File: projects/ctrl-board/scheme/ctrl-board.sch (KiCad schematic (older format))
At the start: 121 parts, among them K1 i2c-1, K2 i2c-1, P1 PWR-IN, P2 CONN_4, P3 PWR-IN, P4 PWR-IN, P5 PWR-IN, P6 CONN_4, P7 CONN_4, P8 PWR-IN, Q1 BC847, Q10 BC847, Q11 MOS_P, Q12 MOS_P, Q13 MOS_P, Q2 BC847, Q3 BC847, Q4 BC857, Q5 MOS_P, Q6 MOS_N, Q7 BC847, Q8 BC847, Q9 BC857, U1 NCP3063, U2 L293, X1 8MHz

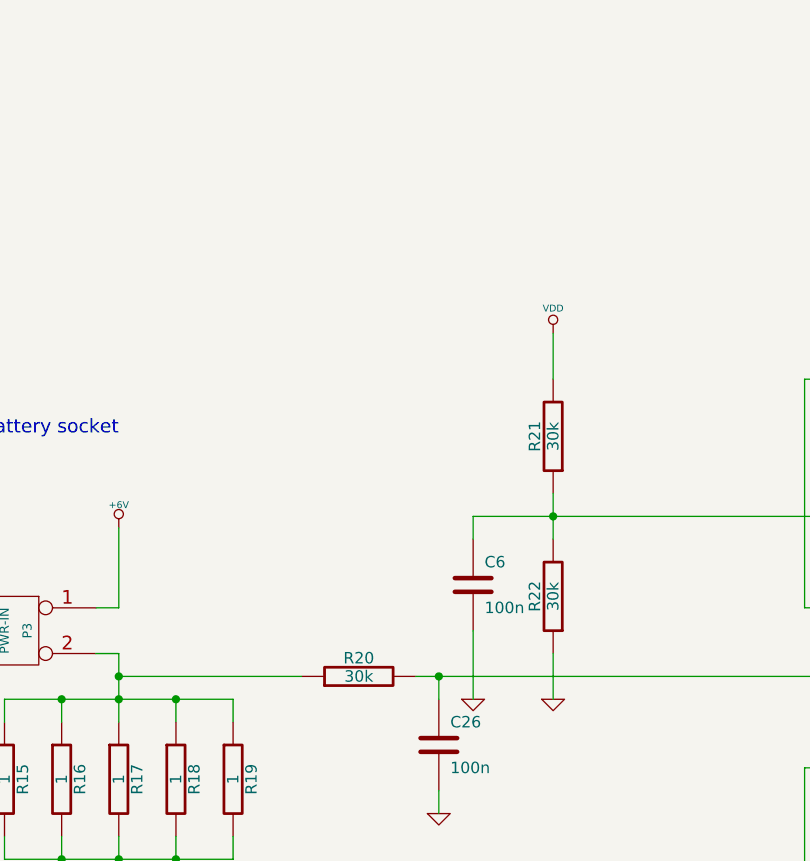
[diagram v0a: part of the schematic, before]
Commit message: Rerouted with eliminating error with measuring consuming current.
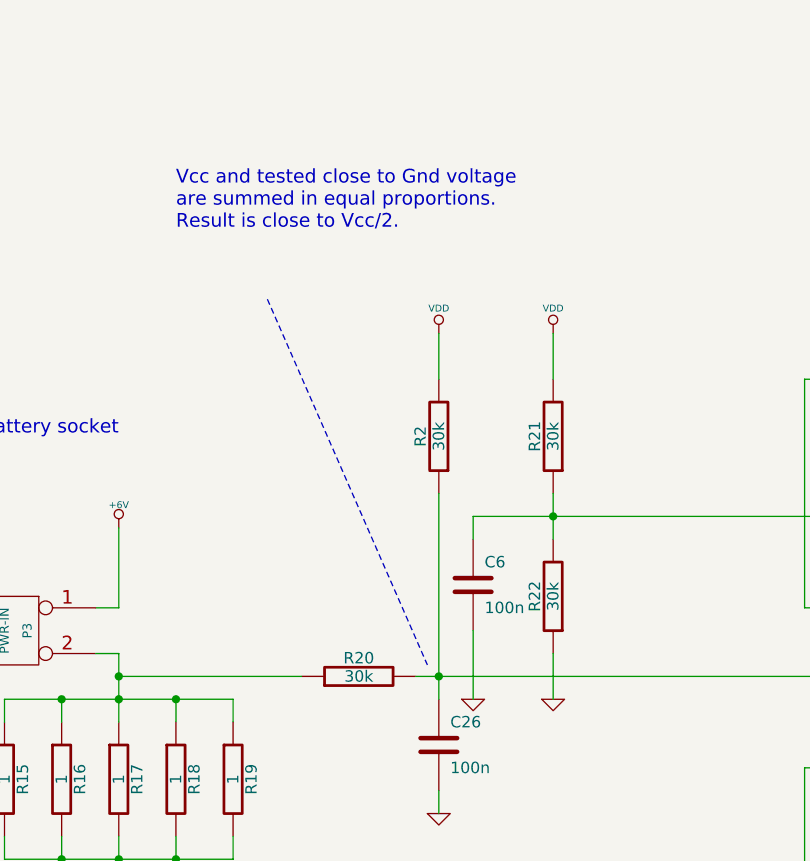
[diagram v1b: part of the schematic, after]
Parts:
- added R2: 30k, symbol R
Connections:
- wire segments 367 -> 368
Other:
- note added: "Vcc and tested close to Gnd voltage \nare summed in equal proportions. \nResult is close to Vcc/2."
